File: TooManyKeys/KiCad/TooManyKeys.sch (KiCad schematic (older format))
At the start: 60 parts, among them J1 54104-3031_Oled, J2 AVR-ISP-6, SW1 SW_Push, U1 PRTR5V0U2X, U2 AT90USB1286-AU, U3 PCA9306, U4 AZ1117CH-3.3TRG1, Y1 16MHz

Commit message: Final Version of Schematic and PCB
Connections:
- no-connect marks 0 -> 17
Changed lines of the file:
@@
 Wire Wire Line
 	11700 8100 11400 8100
+NoConn ~ 2900 2000
+NoConn ~ 4100 2300
+NoConn ~ 4100 2700
+NoConn ~ 4100 2800
+NoConn ~ 4100 2900
+NoConn ~ 4100 3000
+NoConn ~ 2900 3500
+NoConn ~ 2900 3600
+NoConn ~ 2900 3700
+NoConn ~ 4100 1400
+NoConn ~ 4100 4300
+NoConn ~ 4100 4400
+NoConn ~ 4100 4500
+NoConn ~ 4100 4600
+NoConn ~ 10900 1700
+NoConn ~ 6150 1950
+NoConn ~ 6150 2550
 $EndSCHEMATC

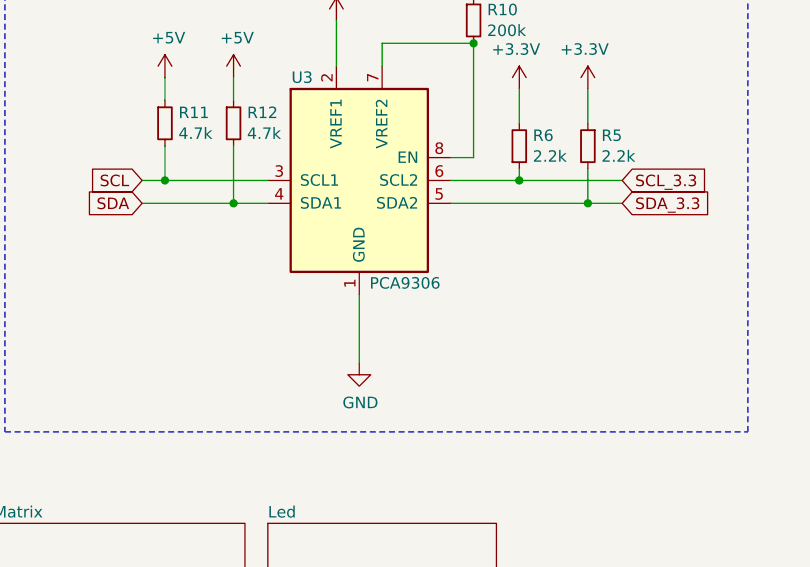
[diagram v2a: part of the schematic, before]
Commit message: Set Led footprint text position
Renaming items in footprint library
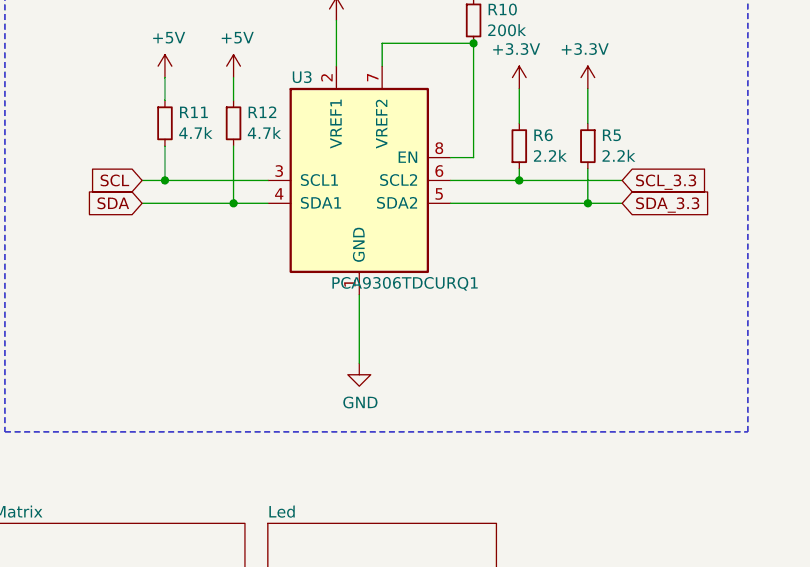
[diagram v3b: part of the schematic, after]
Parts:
- U3: value PCA9306 -> PCA9306TDCURQ1
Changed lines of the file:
@@
 P 2250 8300
 F 0 "U3" H 2000 8750 50  0000 C CNN
-F 1 "PCA9306" H 2450 7850 50  0000 C CNN
+F 1 "PCA9306TDCURQ1" H 2450 7850 50  0000 C CNN
 F 2 "SamacSys_Parts:SOP50P310X90-8N" H 1850 8650 50  0001 C CNN
 F 3 "http://www.ti.com/lit/ds/symlink/pca9306.pdf" H 1950 8750 50  0001 C CNN

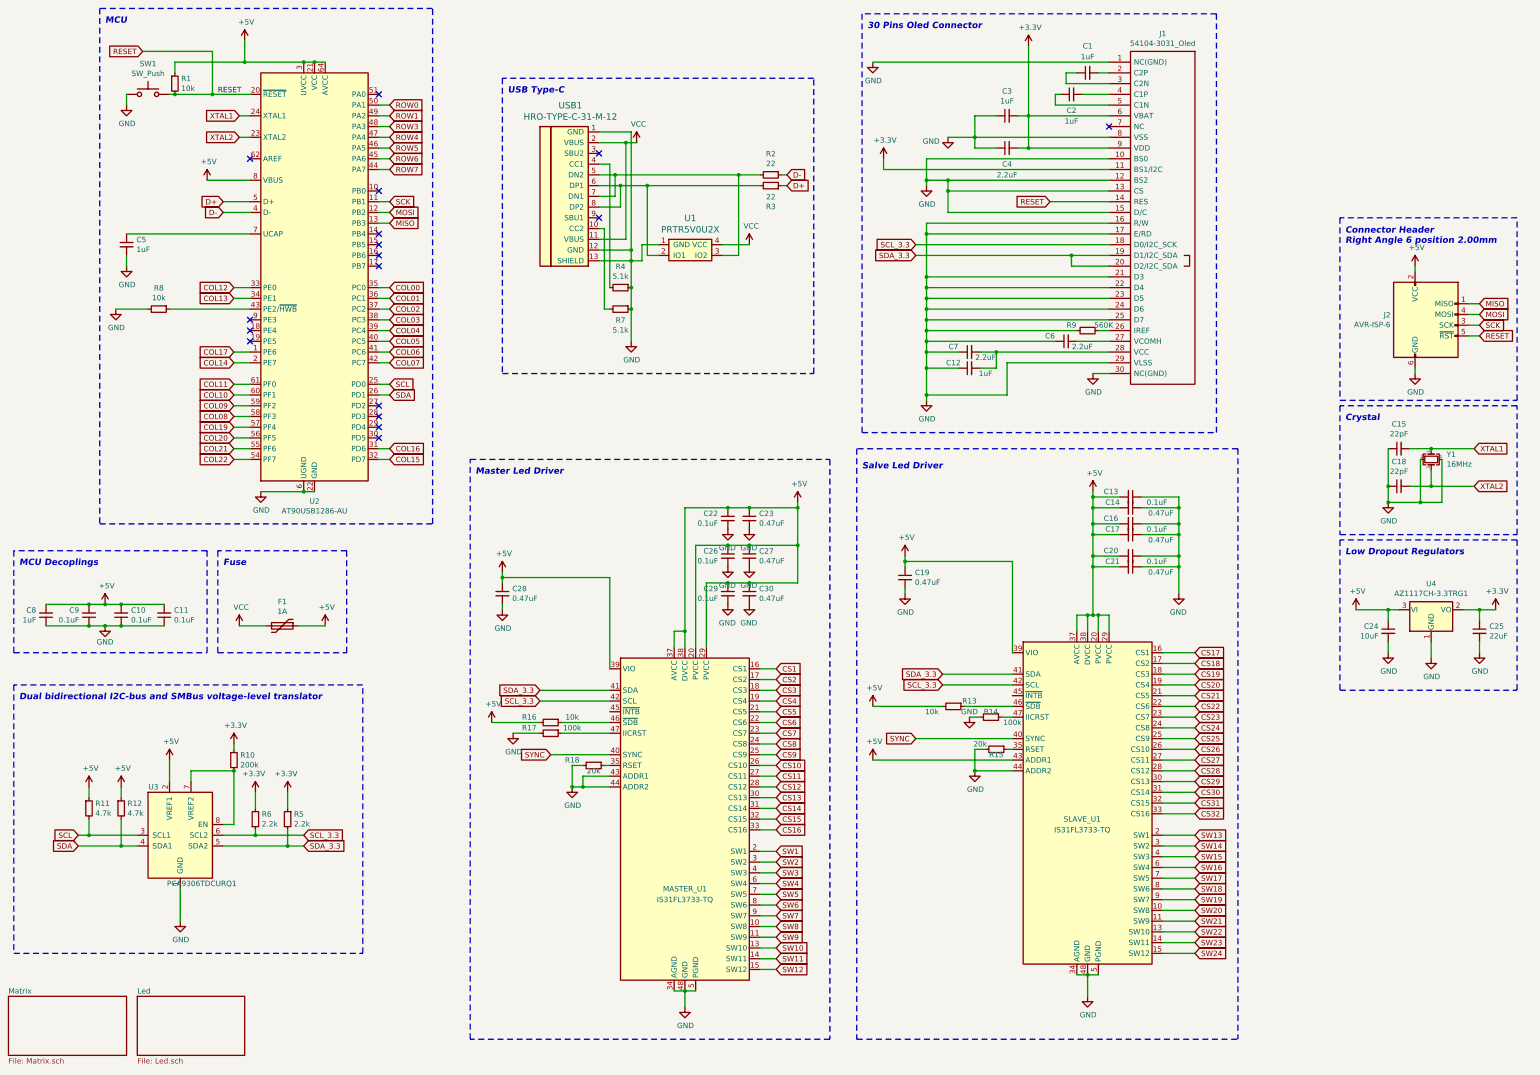
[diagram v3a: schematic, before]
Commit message: Changes following contractor review( ressources / Schematic Review.docx )
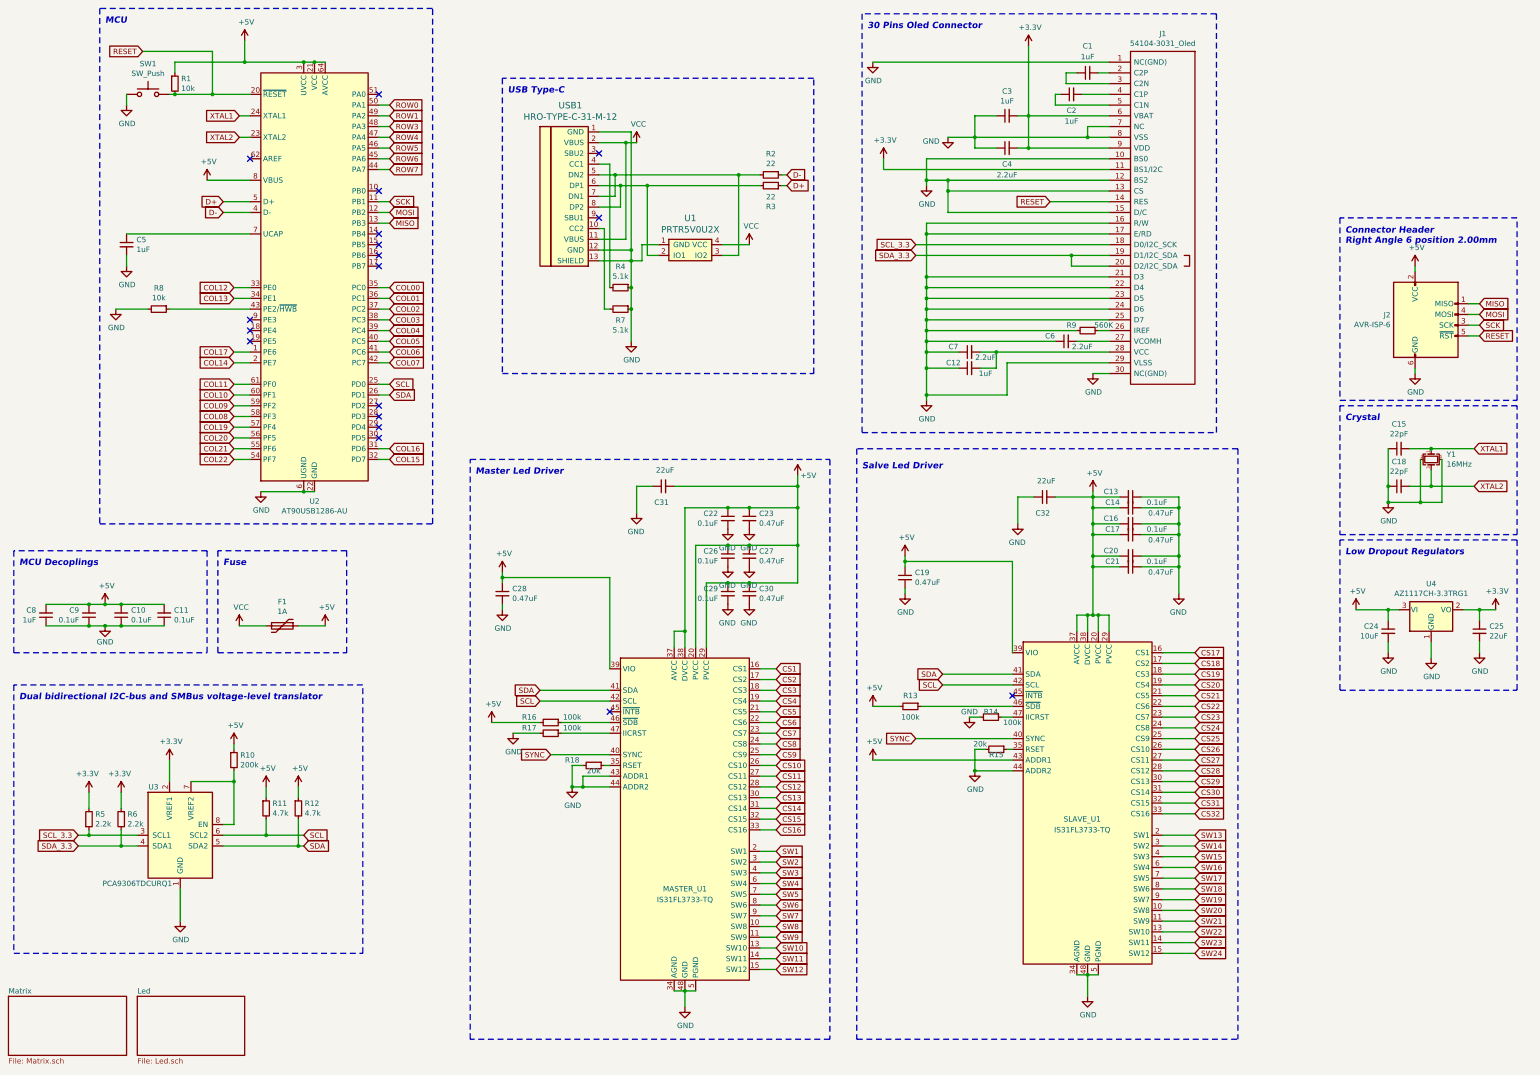
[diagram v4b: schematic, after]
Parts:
- added C31, C32: 22uF, Capacitor_SMD:C_0805_2012Metric, symbol Device:C_Small
- R13, R16: value 10k -> 100k
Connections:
- net +3V3: now also R5.2, R6.1, U3.2 (VREF1); no longer R10.1, R5.1, R6.2
- net +5V: now also R10.1, C31.2, C32.2; no longer U3.2 (VREF1)
- net GND: now also J1.7 (NC), C31.1, C32.1
- net SCL: now also MASTER_U1.42 (SCL), SLAVE_U1.42 (SCL), U3.6 (SCL2); no longer U3.3 (SCL1)
- net SCL_3.3: now also R5.1, U3.3 (SCL1); no longer MASTER_U1.42 (SCL), R6.1, SLAVE_U1.42 (SCL), U3.6 (SCL2)
- net SDA: now also MASTER_U1.41 (SDA), SLAVE_U1.41 (SDA), U3.5 (SDA2); no longer U3.4 (SDA1)
- net SDA_3.3: now also R6.2, U3.4 (SDA1); no longer MASTER_U1.41 (SDA), R5.2, SLAVE_U1.41 (SDA), U3.5 (SDA2)
- no-connect marks 17 -> 18
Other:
- moved on the sheet: R11, R12, R13
